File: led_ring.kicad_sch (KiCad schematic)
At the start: 24 parts

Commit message: Improve page title
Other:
- company: (none) -> https://github.com/pedalboard
- title: (none) -> Pedalboard Dispaly
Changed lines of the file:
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@@
 	(paper "A4")
 	(title_block
-		(date "2024-10-04")
+		(title "Pedalboard Dispaly")
+		(date "2024-10-05")
 		(rev "0.0.0-RC1")
+		(company "https://github.com/pedalboard")
+		(comment 1 "Source Code: https://github.com/pedalboard/pedalboard-display")
+		(comment 2 "License: CERN Open Hardware Licence Version 2 - Permissive")
+		(comment 3 "Git commit: ${GIT_HASH}")
 	)
 	(junction

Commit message: Fix title
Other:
- title: Pedalboard Dispaly -> Pedalboard Display
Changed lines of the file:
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@@
 	(paper "A4")
 	(title_block
-		(title "Pedalboard Dispaly")
+		(title "Pedalboard Display")
 		(date "2024-10-05")
 		(rev "0.0.0-RC1")

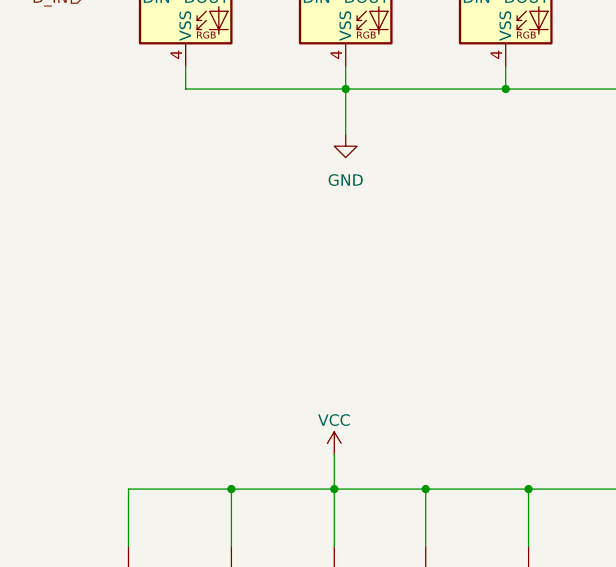
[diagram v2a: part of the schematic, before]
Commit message: Add actuators 3d models
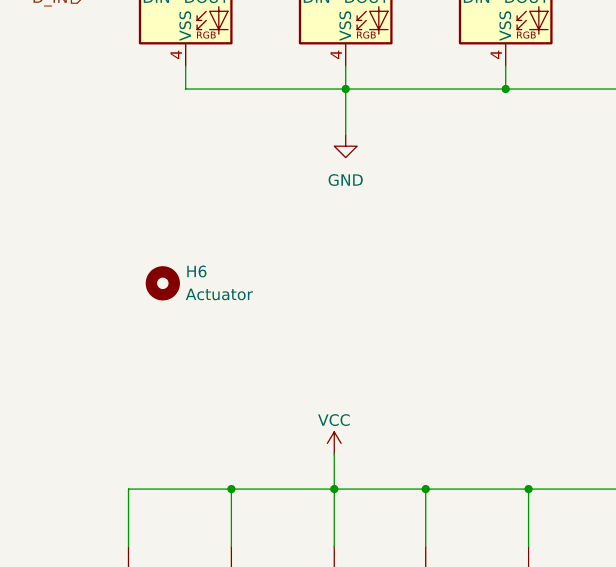
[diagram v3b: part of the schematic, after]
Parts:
- added H6: Actuator, Library:Actuator, symbol Mechanical:MountingHole
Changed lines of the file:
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@@
+	)
+	(symbol
+		(lib_id "Mechanical:MountingHole")
+		(at 49.53 83.82 0)
+		(unit 1)
+		(exclude_from_sim yes)
+		(in_bom no)
+		(on_board yes)
+		(dnp no)
+		(fields_autoplaced yes)
+		(property "Reference" "H6"
+			(at 52.07 82.5499 0)
+			(effects
+				(font
+					(size 1.27 1.27)
+				)
+				(justify left)
+			)
+		)
+		(property "Value" "Actuator"
+			(at 52.07 85.0899 0)
+			(effects
+				(font
+					(size 1.27 1.27)
+				)
+				(justify left)
+			)
+		)
+		(property "Footprint" "Library:Actuator"
+			(at 49.53 83.82 0)
+			(effects
+				(font
+					(size 1.27 1.27)
+				)
+				(hide yes)
+			)
+		)
+		(property "Datasheet" "~"
+			(at 49.53 83.82 0)
+			(effects
+				(font
+					(size 1.27 1.27)
+				)
+				(hide yes)
+			)
+		)
+		(property "Description" "Mounting Hole without connection"
+			(at 49.53 83.82 0)
+			(effects
+				(font
+					(size 1.27 1.27)
+				)
+				(hide yes)
+			)
+		)
+		(instances
+			(project ""
+				(path "/02aefeb1-bdda-4e04-a64a-6cb1fcf66702/03a1be90-6662-4c1b-aea8-af89ab9fe3ff"
+					(reference "H6")
+					(unit 1)
+				)
+				(path "/02aefeb1-bdda-4e04-a64a-6cb1fcf66702/60bcd1af-a60a-4f55-975b-2d52ed6bc101"
+					(reference "H8")
+					(unit 1)
+				)
+				(path "/02aefeb1-bdda-4e04-a64a-6cb1fcf66702/8686615e-b239-440c-93c8-70026f9bbbfb"
+					(reference "H10")
+					(unit 1)
+				)
+				(path "/02aefeb1-bdda-4e04-a64a-6cb1fcf66702/9f368d8b-0a33-48ea-87fd-73a39b4ae17d"
+					(reference "H12")
+					(unit 1)
+				)
+				(path "/02aefeb1-bdda-4e04-a64a-6cb1fcf66702/a611c427-264b-4cbb-a141-70a2759b7fda"
+					(reference "H9")
+					(unit 1)
+				)
+				(path "/02aefeb1-bdda-4e04-a64a-6cb1fcf66702/b1e2b4f6-0ba7-451d-b62b-4dbc4f5ed3b2"
+					(reference "H11")
+					(unit 1)
+				)
+				(path "/02aefeb1-bdda-4e04-a64a-6cb1fcf66702/c00f76d2-ee00-4ab6-af0a-f31a76675e6f"
+					(reference "H7")
+					(unit 1)
+				)
+				(path "/02aefeb1-bdda-4e04-a64a-6cb1fcf66702/c644a370-7604-41fa-a06f-3d12156bb3c9"
+					(reference "H13")
+					(unit 1)
+				)
+			)
+		)
 	)
 	(symbol

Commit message: Use led-ring-encoder-washer
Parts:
- H6: footprint Library:Actuator -> ${ActuatorFootprint}
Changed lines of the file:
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@@
 			)
 		)
-		(property "Footprint" "Library:Actuator"
+		(property "Footprint" "${ActuatorFootprint}"
 			(at 49.53 83.82 0)
 			(effects
